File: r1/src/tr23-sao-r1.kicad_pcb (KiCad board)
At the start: 2 copper layers, 30.5 x 50 mm, 6 parts, among them J1 Conn_02x03_Odd_Even, J2 Conn_01x06_Shielded

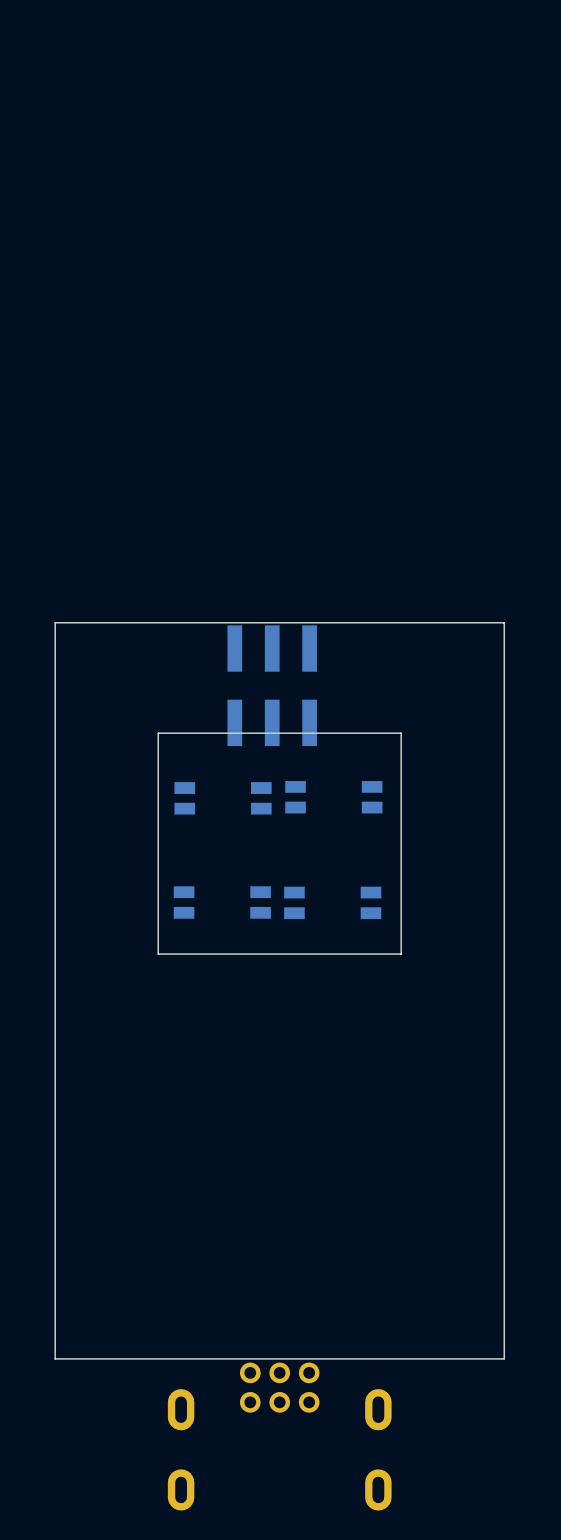
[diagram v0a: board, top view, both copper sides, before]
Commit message: Import latest graphic artwork, place LED's and connectors, define DRC rules
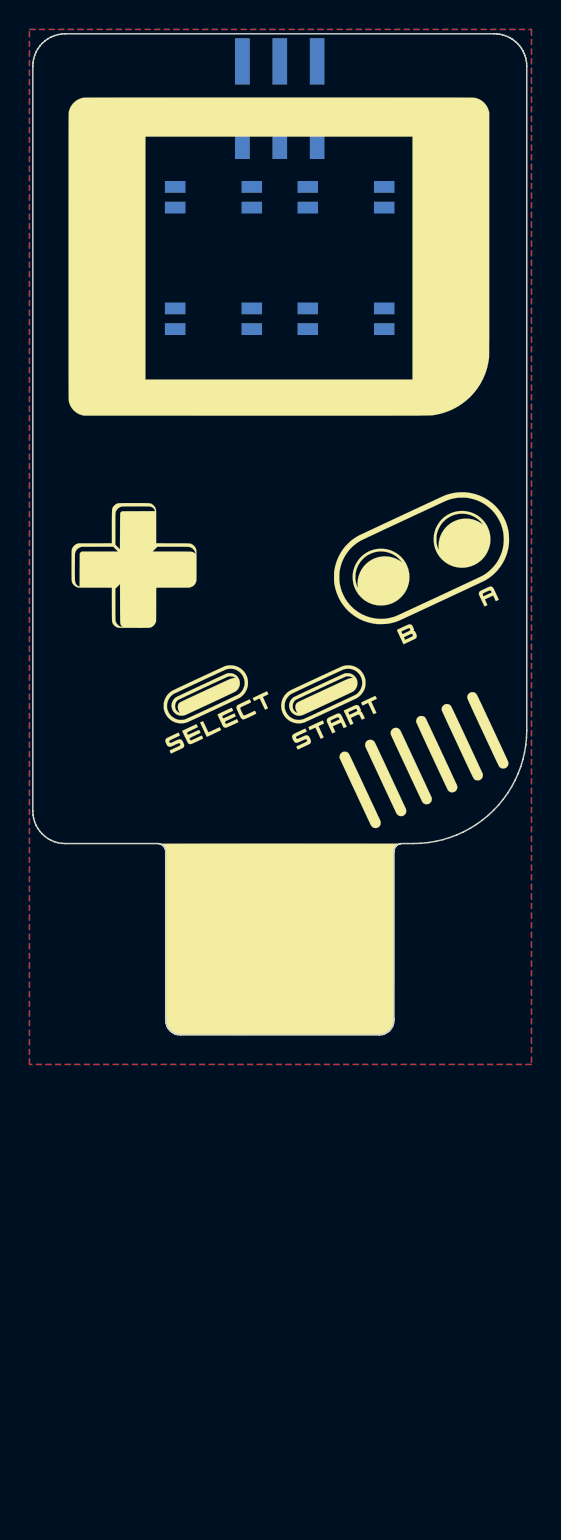
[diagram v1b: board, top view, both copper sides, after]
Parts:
- added GRAPHIC1: ~, tr23-sao:tr23-sao, F.Cu at (156.3, 112.2)
- moved D1 40.8 mm to (145.5, 61.1)
- moved D2 40.8 mm to (154.5, 61.1)
- moved J1 39.9 mm to (150.0, 54.4)
- moved D4 39.7 mm to (154.5, 69.3)
- moved D3 39.7 mm to (145.5, 69.3)
- moved J2 35.1 mm to (150.0, 111.1)
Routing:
- added copper zone on B.Cu, net GND
- added copper zone on F.Cu, net GND
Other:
- board size 30.5 x 50 mm -> 33.5 x 68 mm

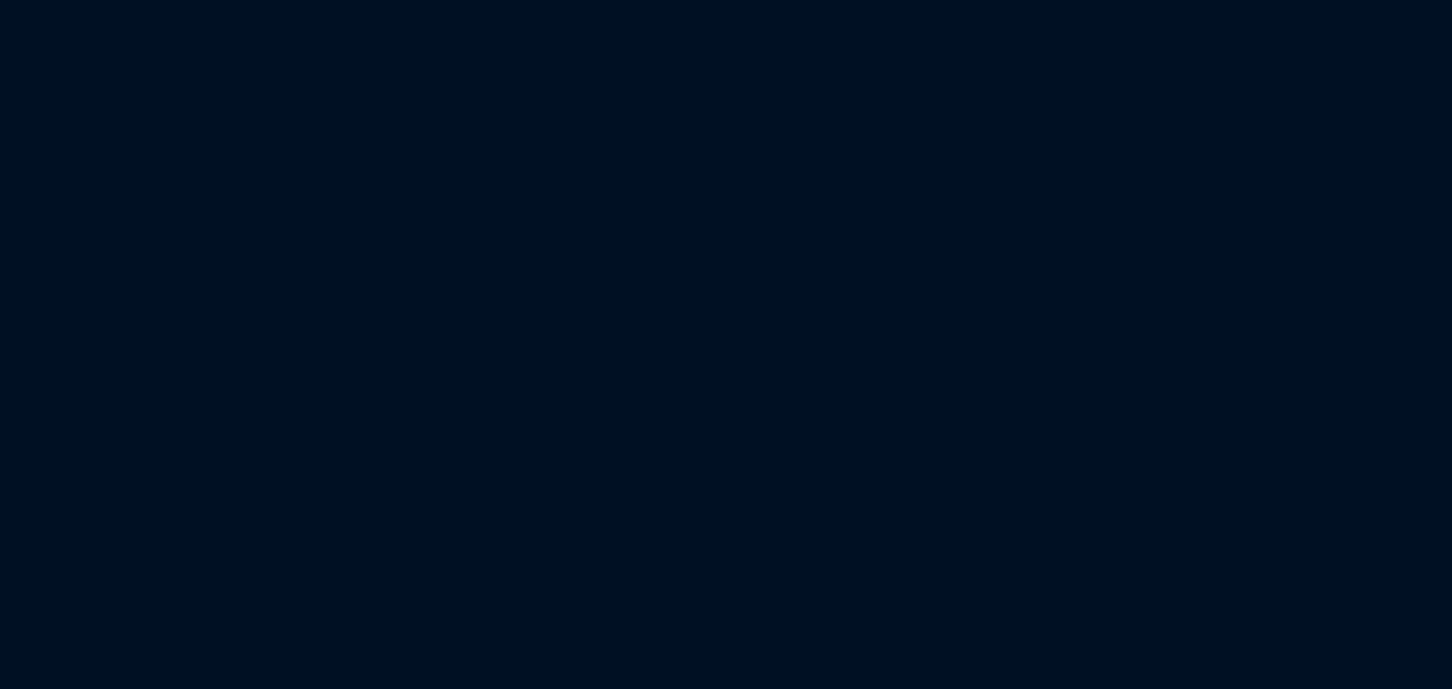
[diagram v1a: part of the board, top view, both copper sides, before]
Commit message: Update LED driver symbol to connect EP pad properly
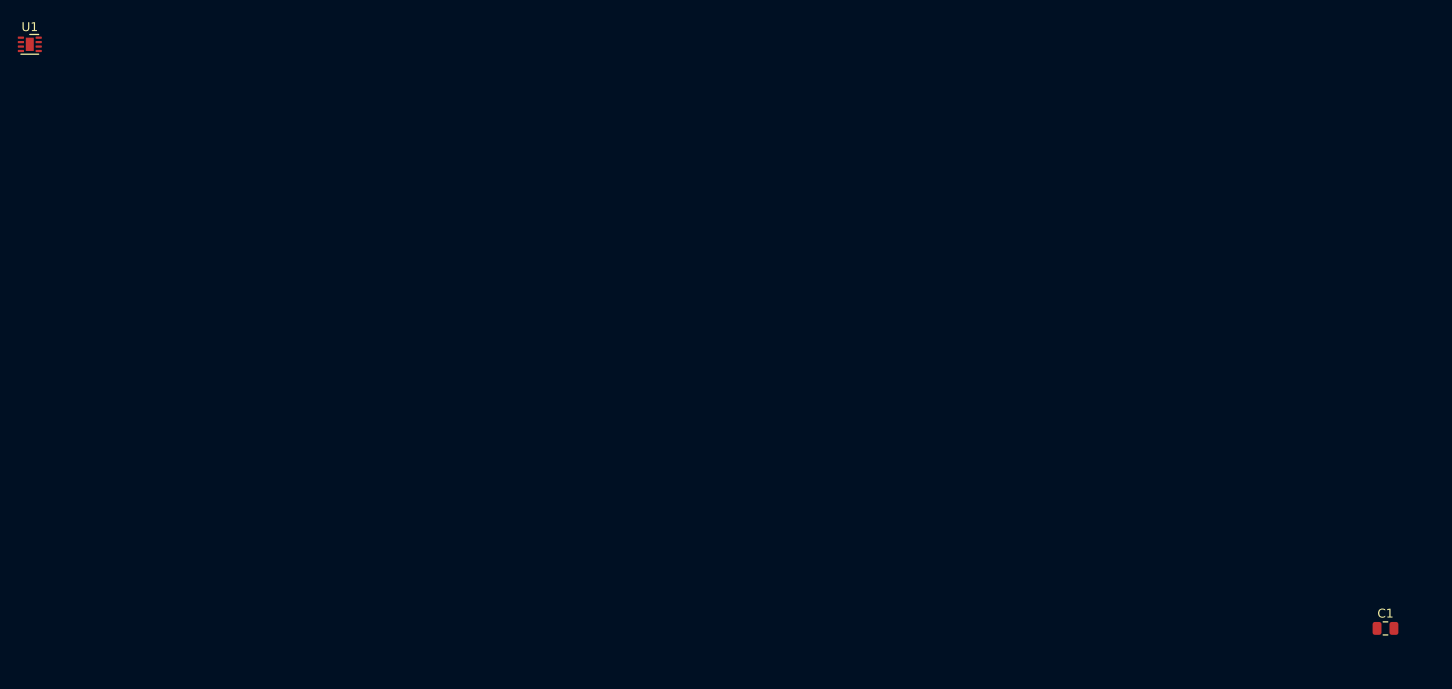
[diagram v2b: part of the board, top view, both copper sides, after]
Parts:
- added C1: 10uF, Capacitor_SMD:C_0805_2012Metric, F.Cu at (119.6, 51.6)
- added U1: ~, Package_DFN_QFN:DFN-8-1EP_2x2mm_P0.5mm_EP0.9x1.5mm, F.Cu at (-32.8, -14.1)
- J2: value Conn_01x06_Shielded -> Wii_Nunchuck_Connector
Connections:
- D1 pad 1: unconnected-(D1-RK-Pad1) -> /LED3
- D1 pad 2: unconnected-(D1-A-Pad2) -> /LED1
- D1 pad 3: unconnected-(D1-BK-Pad3) -> /LED4
- D1 pad 4: unconnected-(D1-GK-Pad4) -> /LED2
- D2 pad 1: unconnected-(D2-RK-Pad1) -> /LED4
- D2 pad 2: unconnected-(D2-A-Pad2) -> /LED2
- D2 pad 3: unconnected-(D2-BK-Pad3) -> /LED1
- D2 pad 4: unconnected-(D2-GK-Pad4) -> /LED3
- D3 pad 1: unconnected-(D3-RK-Pad1) -> /LED1
- D3 pad 2: unconnected-(D3-A-Pad2) -> /LED3
- D3 pad 3: unconnected-(D3-BK-Pad3) -> /LED2
- D3 pad 4: unconnected-(D3-GK-Pad4) -> /LED4
- D4 pad 1: unconnected-(D4-RK-Pad1) -> /LED2
- D4 pad 2: unconnected-(D4-A-Pad2) -> /LED4
- D4 pad 3: unconnected-(D4-BK-Pad3) -> /LED3
- D4 pad 4: unconnected-(D4-GK-Pad4) -> /LED1
- J1 pad 5: /IO1 -> unconnected-(J1-Pin_5-Pad5)
- J1 pad 6: /IO2 -> GND
- J2 pad 1: unconnected-(J2-Pin_1-Pad1) -> /SDA
- J2 pad 3: unconnected-(J2-Pin_3-Pad3) -> +3V3
- J2 pad 4: unconnected-(J2-Pin_4-Pad4) -> /SCL
- J2 pad 6: unconnected-(J2-Pin_6-Pad6) -> GND
- J2 pad SH: unconnected-(J2-Shield-PadSH) -> GND

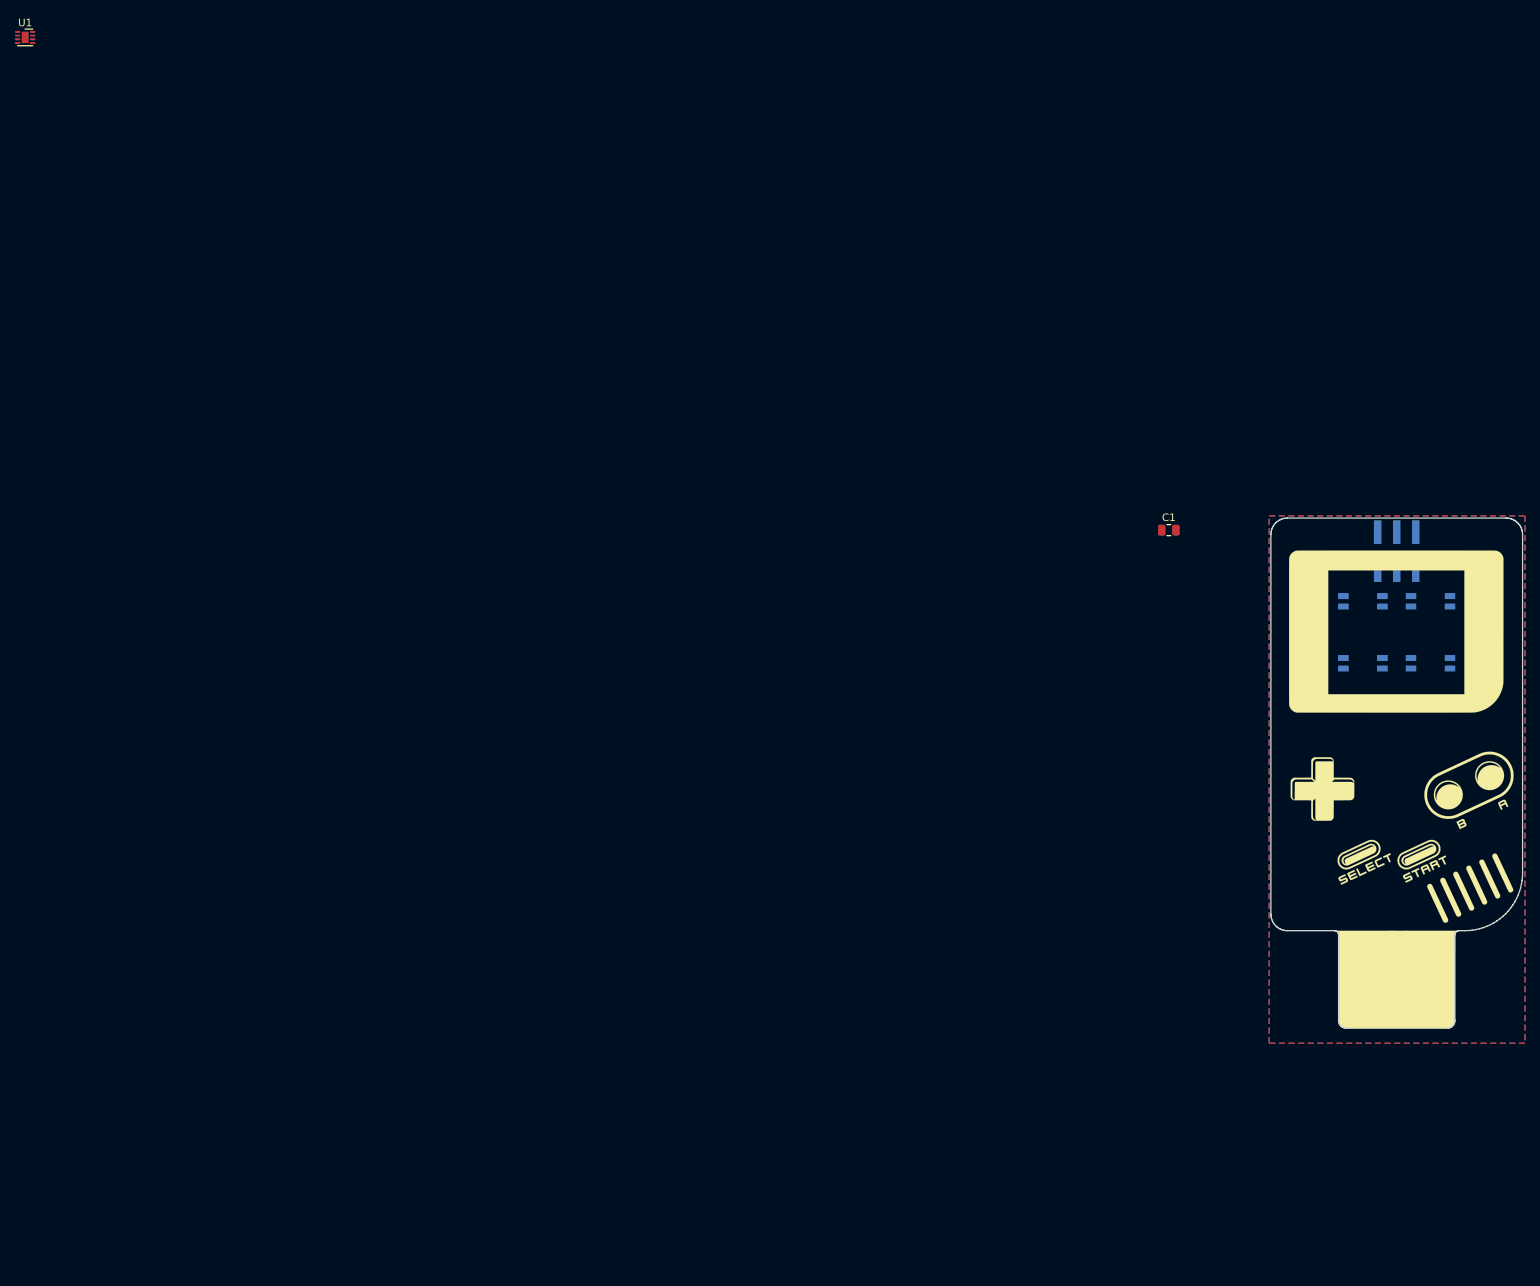
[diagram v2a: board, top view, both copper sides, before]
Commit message: Route LEDs
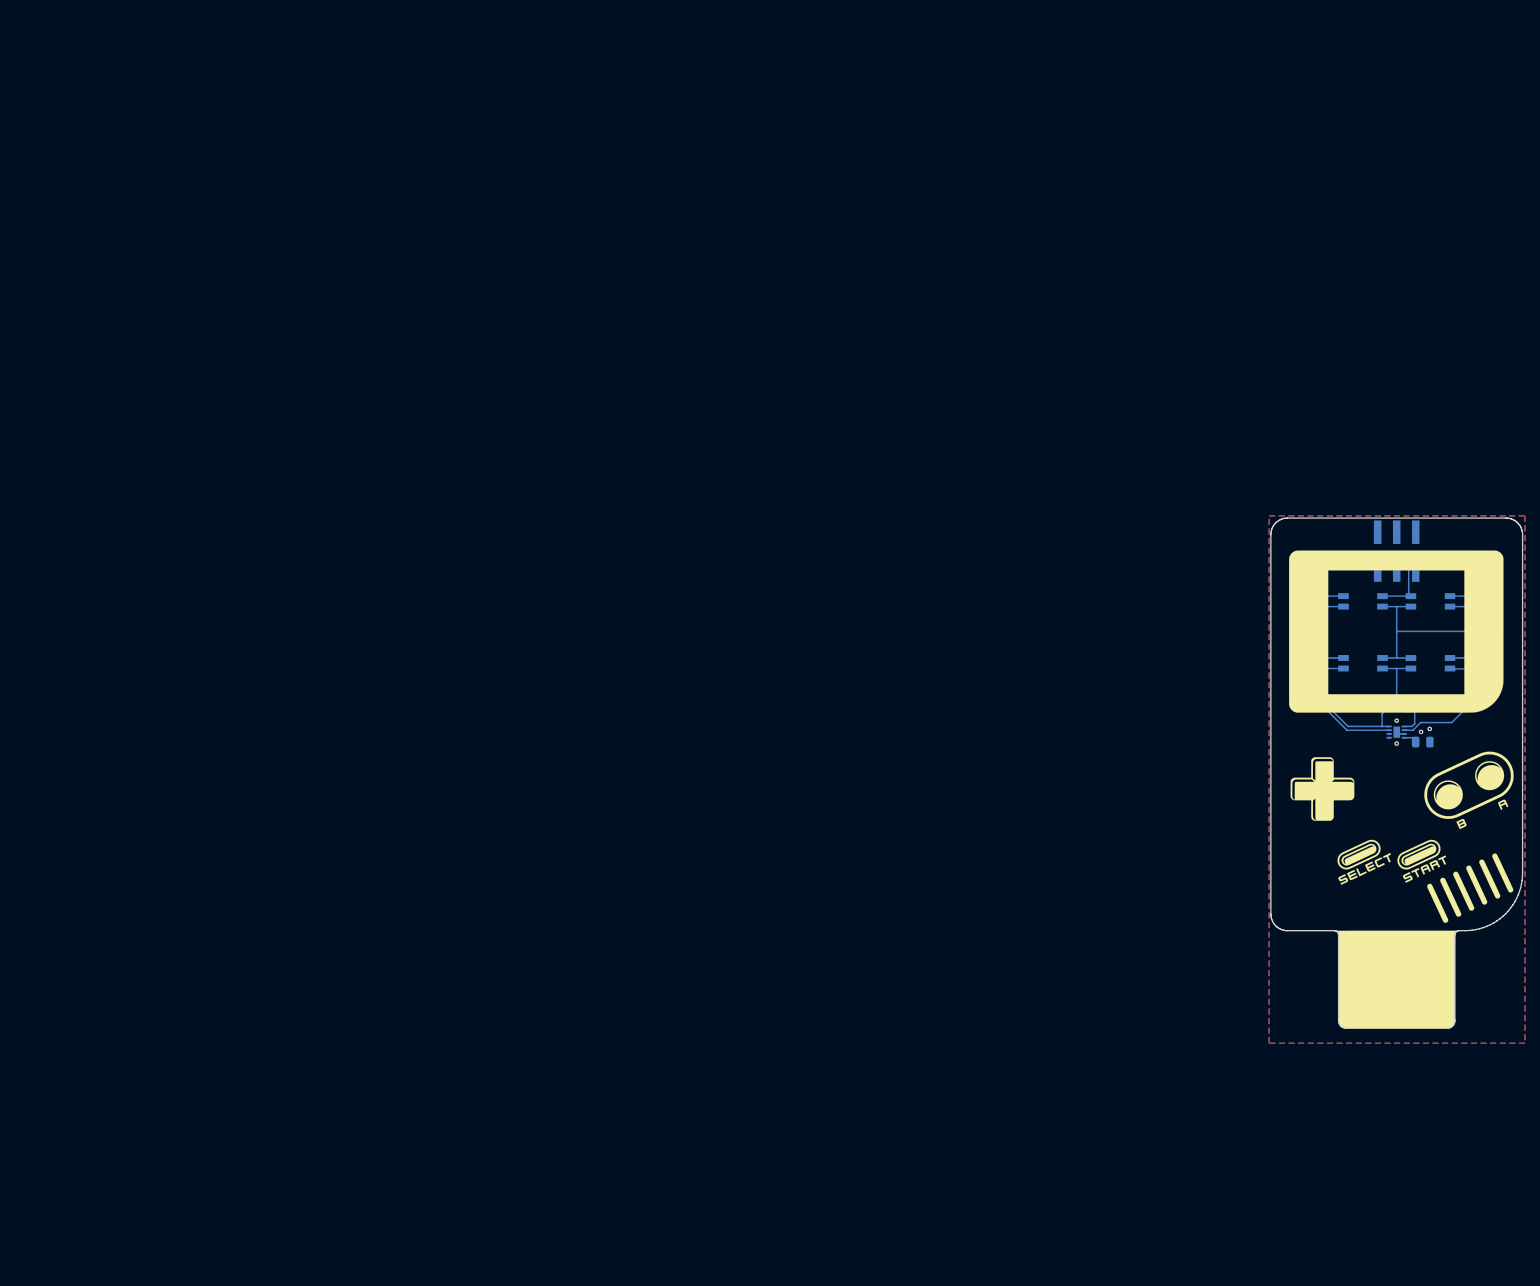
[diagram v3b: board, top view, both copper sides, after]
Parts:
- C1, U1: moved to B.Cu
- moved U1 204.9 mm to (150.0, 78.5)
- moved C1 44.1 mm to (153.5, 79.9)
- moved D1 9.00 mm to (154.5, 61.1)
- moved D4 9.00 mm to (145.5, 69.3)
- moved D2 8.25 mm to (154.5, 69.3)
- moved D3 8.25 mm to (145.5, 61.1)
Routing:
- net /LED2: track 0.00 -> 67.4 mm
- net /LED3: track 0.00 -> 63.9 mm, vias 0 -> 4
- net /LED4: track 0.00 -> 59.1 mm, vias 0 -> 4
- net /LED1: track 0.00 -> 47.9 mm, vias 0 -> 2
- net +3V3: track 0.00 -> 2.11 mm
- net GND: track 0.00 -> 1.10 mm, vias 0 -> 4

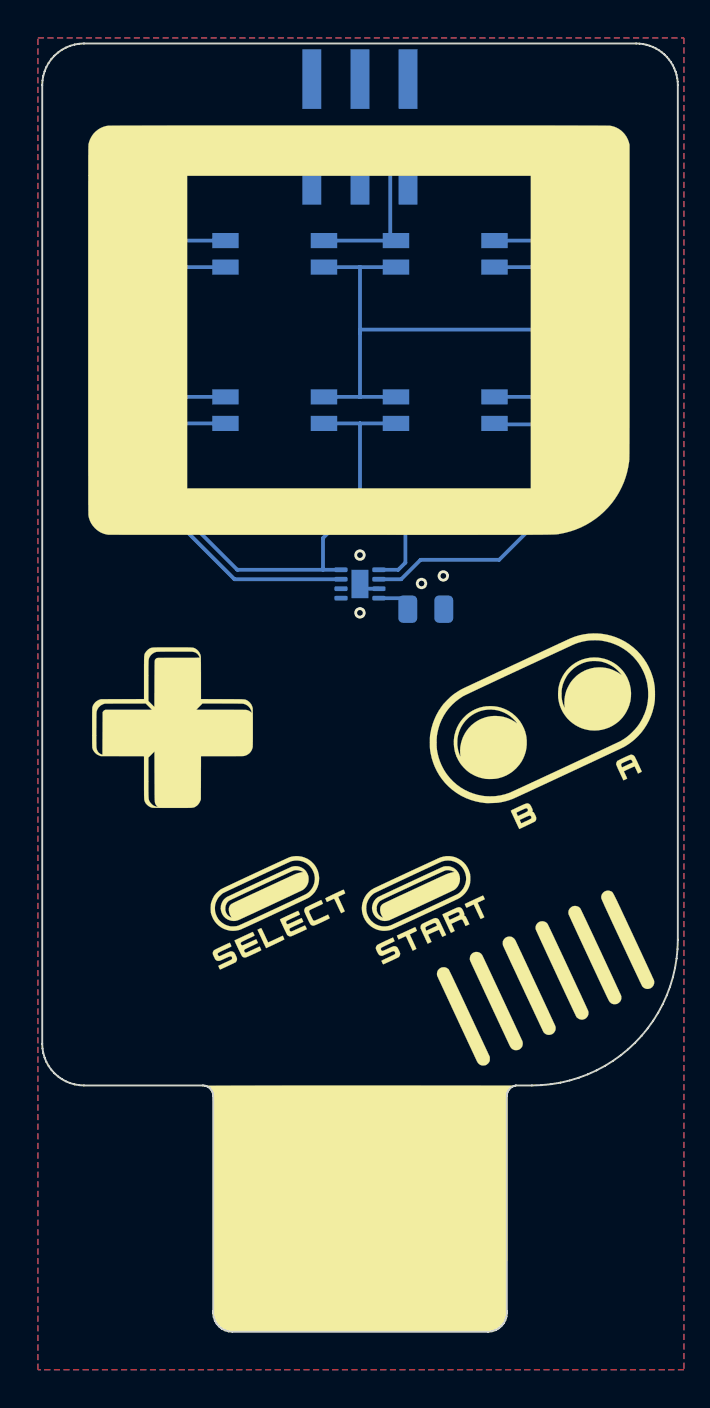
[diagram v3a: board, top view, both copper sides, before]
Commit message: Add graphics to rear silk. Set drawing titles.
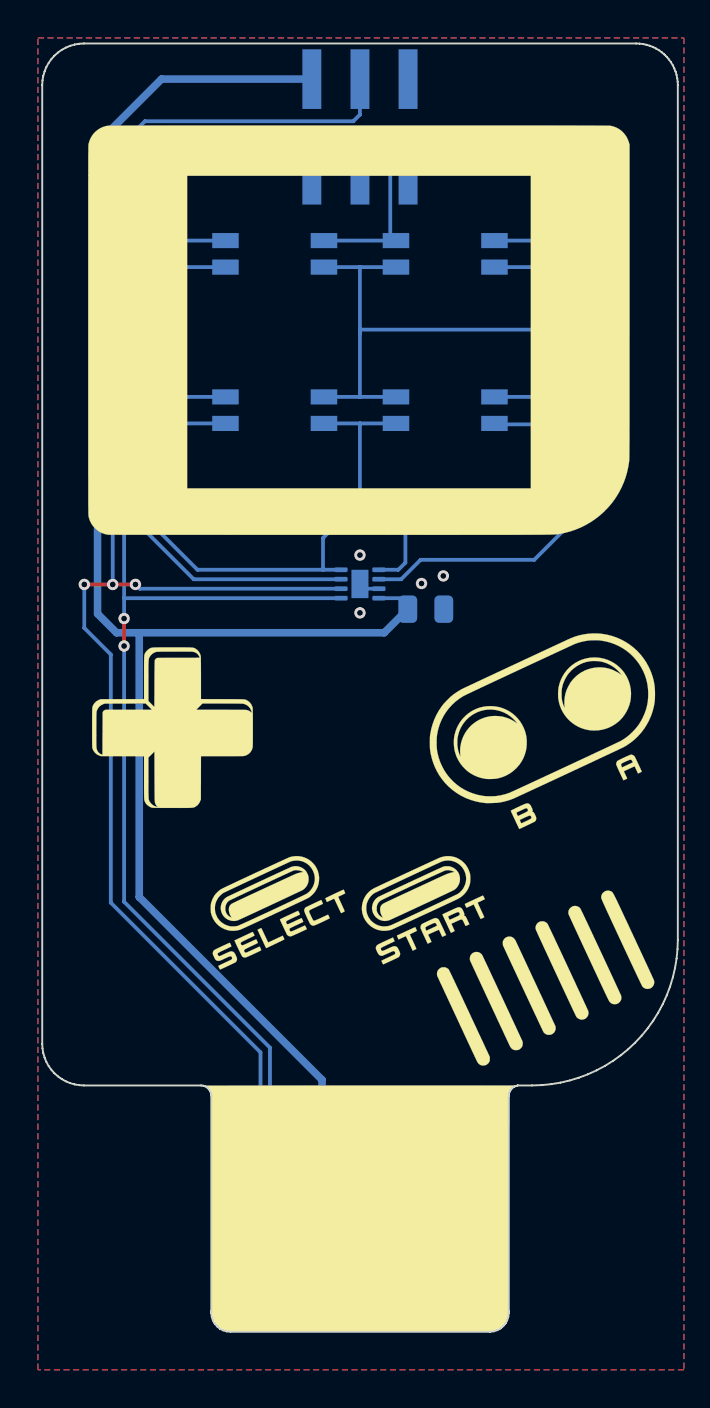
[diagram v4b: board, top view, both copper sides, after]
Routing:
- net /SDA: track 0.00 -> 98.9 mm, vias 0 -> 3
- net +3V3: track 2.11 -> 85.8 mm
- net /SCL: track 0.00 -> 82.6 mm, vias 0 -> 2
- net /LED4: track 59.1 -> 87.3 mm, vias 4 -> 6
- net /LED3: track 63.9 -> 65.3 mm
- net /LED1: track 47.9 -> 49.0 mm
- net GND: vias 4 -> 8
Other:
- outline, holes or cut-outs redrawn
- board text added: "D1 D3 D2 D4"
- board text added: "J2 Mount connector other side"
